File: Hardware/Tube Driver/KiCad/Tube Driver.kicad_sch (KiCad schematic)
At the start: 45 parts, among them J1 I/O, Q1 MMBT3904, Q2 STN2580, Q3 MMBT3904, Q4 MMBT3906, U1 NE555D

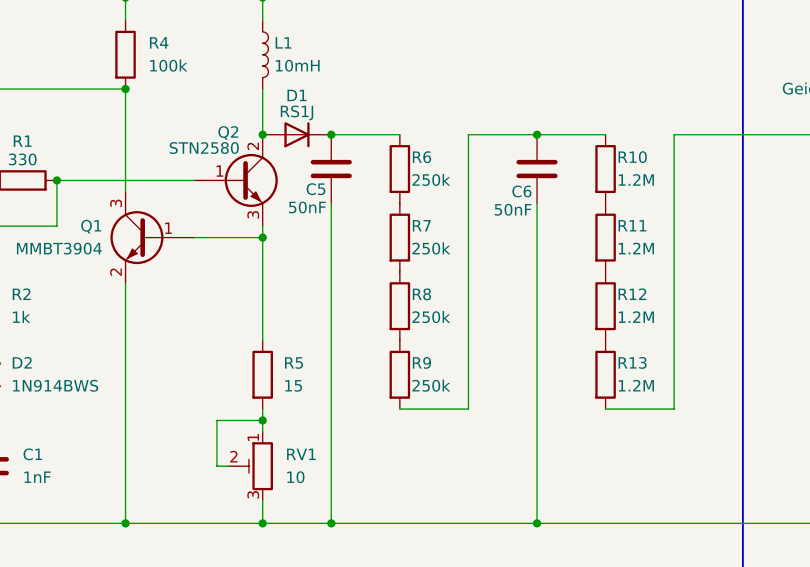
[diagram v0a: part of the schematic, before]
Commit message: Added BoM, updated component values and PCB
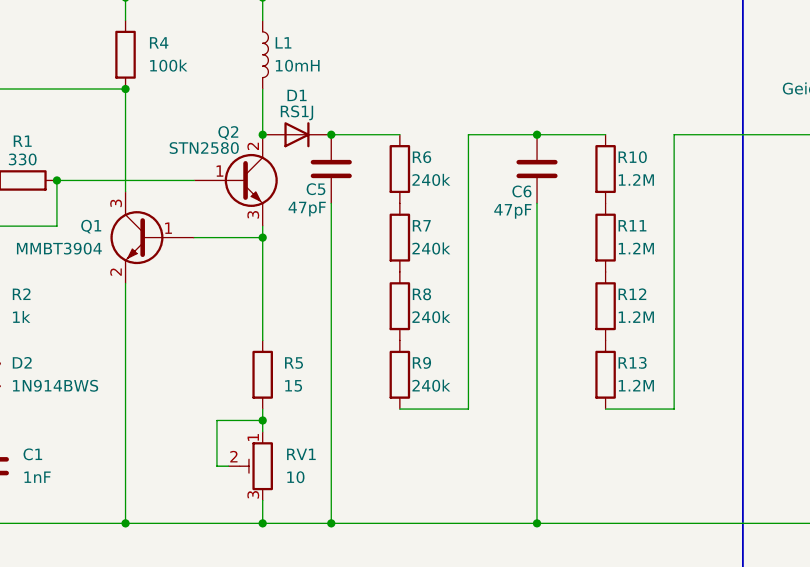
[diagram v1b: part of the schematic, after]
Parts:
- C1: DigiKey (none) -> https://www.digikey.com/en/products/detail/w%C3%BCrth-elekt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; MPN (none) -> 885012208046; Price (EUR) (none) -> 0,09€
- C2, C3: DigiKey (none) -> https://www.digikey.com/en/products/detail/w%C3%BCrth-elekt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; MPN (none) -> 885012208112; Price (EUR) (none) -> 0,1€
- C4: DigiKey (none) -> https://www.digikey.com/en/products/detail/w%C3%BCrth-elekt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; MPN (none) -> 865080243007; Price (EUR) (none) -> 0,25€
- C5, C6: value 50nF -> 47pF; footprint Capacitor_SMD:C_1206_3216Metric_Pad1.33x1.80mm_HandSolder -> Capacitor_SMD:C_1210_3225Metric_Pad1.33x2.70mm_HandSolder; DigiKey (none) -> https://www.digikey.com/en/products/detail/kemet/C1210V473K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; MPN (none) -> C1210V473KDRAC7800; Price (EUR) (none) -> 0,31€
- C7: DigiKey (none) -> https://www.digikey.com/en/products/detail/yageo/CC1206FRNP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; MPN (none) -> CC1206FRNPO9BN821; Price (EUR) (none) -> 0,45€
- D1: DigiKey (none) -> https://www.digikey.com/en/products/detail/diodes-incorpora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; MPN (none) -> RS1J-13-F; Price (EUR) (none) -> 0,4€
- D2: DigiKey (none) -> https://www.digikey.com/en/products/detail/onsemi/1N914BWS/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; MPN (none) -> 1N914BWS; Price (EUR) (none) -> 0,14€
- D3: DigiKey (none) -> https://www.digikey.com/en/products/detail/panjit-internati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; MPN (none) -> RB751V-40_R1_00001; Price (EUR) (none) -> 0,14€
- D4: DigiKey (none) -> https://www.digikey.com/en/products/detail/w%C3%BCrth-elekt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; MPN (none) -> 150120GS75000; Price (EUR) (none) -> 0,2€
- D5: DigiKey (none) -> https://www.digikey.com/en/products/detail/w%C3%BCrth-elekt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; MPN (none) -> 150120RS75000; Price (EUR) (none) -> 0,2€
- GM1: DigiKey (none) -> https://www.digikey.com/en/products/detail/bel-fuse-inc/FC-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; MPN (none) -> FC-102 BRIGHT TIN; Price (EUR) (none) -> 0,1€
- J1: DigiKey (none) -> https://www.digikey.com/en/products/detail/adam-tech/PH2-06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; MPN (none) -> PH2-06-UA; Price (EUR) (none) -> 0,11€
- L1: DigiKey (none) -> https://www.digikey.com/en/products/detail/w%C3%BCrth-elekt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; MPN (none) -> 74404086103; Price (EUR) (none) -> 1,13€
- Q1, Q3: DigiKey (none) -> https://www.digikey.com/en/products/detail/good-ark-semicon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; MPN (none) -> MMBT3904; Price (EUR) (none) -> 0,09€
- Q2: DigiKey (none) -> https://www.digikey.com/en/products/detail/stmicroelectroni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; MPN (none) -> STN2580; Price (EUR) (none) -> 0,48€
- Q4: DigiKey (none) -> https://www.digikey.com/en/products/detail/good-ark-semicon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; MPN (none) -> MMBT3906; Price (EUR) (none) -> 0,09€
- R1: DigiKey (none) -> https://www.digikey.com/en/products/detail/yageo/RC1206FR-0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; MPN (none) -> RC1206FR-07330RL; Price (EUR) (none) -> 0,09€
- R10, R11, R12, R13: DigiKey (none) -> https://www.digikey.com/en/products/detail/yageo/RC1206FR-0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; MPN (none) -> RC1206FR-071M2L; Price (EUR) (none) -> 0,09€
- R14, R15: DigiKey (none) -> https://www.digikey.com/en/products/detail/yageo/RC1206FR-0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; MPN (none) -> RC1206FR-0722KL; Price (EUR) (none) -> 0,09€
- R16, R17, R19: DigiKey (none) -> https://www.digikey.com/en/products/detail/yageo/RC1206FR-1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; MPN (none) -> RC1206FR-1310KL; Price (EUR) (none) -> 0,09€
- R18: DigiKey (none) -> https://www.digikey.com/en/products/detail/yageo/RC1206FR-1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; MPN (none) -> RC1206FR-13150RL; Price (EUR) (none) -> 0,09€
- R2, R20: DigiKey (none) -> https://www.digikey.com/en/products/detail/yageo/RC1206FR-0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; MPN (none) -> RC1206FR-071KL; Price (EUR) (none) -> 0,09€
- R3: DigiKey (none) -> https://www.digikey.com/en/products/detail/yageo/RC1206FR-0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; MPN (none) -> RC1206FR-07220KL; Price (EUR) (none) -> 0,09€
- R4: DigiKey (none) -> https://www.digikey.com/en/products/detail/yageo/AC1206FR-0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; MPN (none) -> AC1206FR-07100KL; Price (EUR) (none) -> 0,09€
- R5: DigiKey (none) -> https://www.digikey.com/en/products/detail/yageo/RC1206FR-0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; MPN (none) -> RC1206FR-0715RL; Price (EUR) (none) -> 0,09€
- R6, R7, R8, R9: value 250k -> 240k; DigiKey (none) -> https://www.digikey.com/en/products/detail/yageo/RC1206FR-0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; MPN (none) -> RC1206FR-07240KL; Price (EUR) (none) -> 0,09€
- RV1: DigiKey (none) -> https://www.digikey.com/en/products/detail/bourns-inc/3361P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; MPN (none) -> 3361P-1-100GLF; Price (EUR) (none) -> 1,14€
- U1: DigiKey (none) -> https://www.digikey.com/en/products/detail/texas-instrument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; MPN (none) -> NE555D; Price (EUR) (none) -> 0,89€

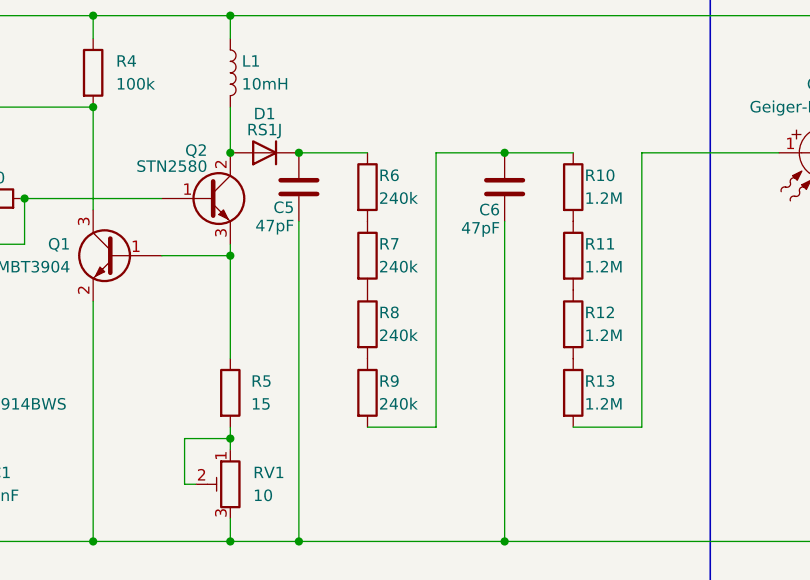
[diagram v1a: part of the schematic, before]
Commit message: Fixed component value typo
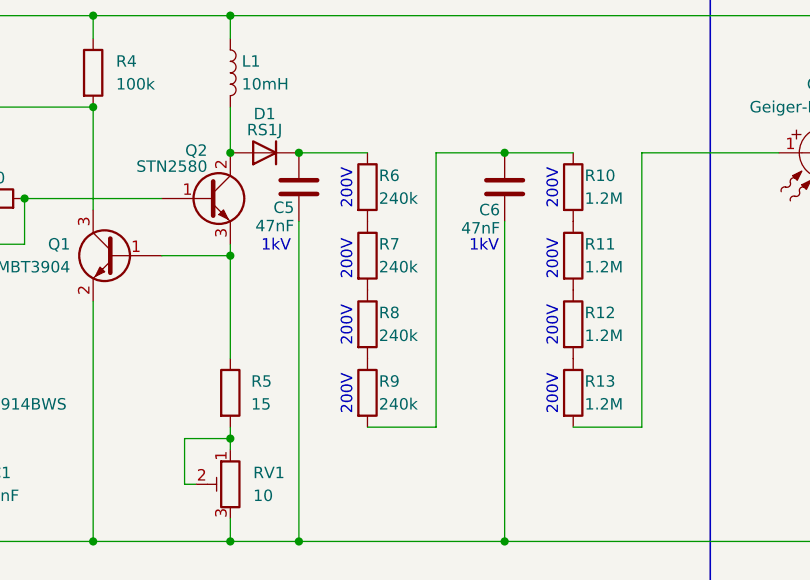
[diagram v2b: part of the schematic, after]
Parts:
- C5, C6: value 47pF -> 47nF
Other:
- note added: "1kV"
- note added: "200V"
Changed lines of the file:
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@@
 	(title_block
 		(title "Tube Driver")
-		(date "2024-09-06")
+		(date "2024-09-10")
 		(rev "1.0")
 		(company "https://github.com/median-dispersion/GMT-Geiger-Counter")
@@
 		)
 	)
+	(text "200V"
+		(exclude_from_sim no)
+		(at 150.114 58.928 90)
+		(effects
+			(font
+				(size 1.27 1.27)
+				(color 0 100 100 1)
+			)
+		)
+	)
+	(text "1kV"
+		(exclude_from_sim no)
+		(at 119.38 57.404 0)
+		(effects
+			(font
+				(size 1.27 1.27)
+				(color 0 100 100 1)
+			)
+		)
+	)
 	(text "GMT"
 		(exclude_from_sim no)
@@
 		)
 	)
+	(text "200V"
+		(exclude_from_sim no)
+		(at 150.114 73.914 90)
+		(effects
+			(font
+				(size 1.27 1.27)
+				(color 0 100 100 1)
+			)
+		)
+	)
+	(text "200V"
+		(exclude_from_sim no)
+		(at 127.254 66.294 90)
+		(effects
+			(font
+				(size 1.27 1.27)
+				(color 0 100 100 1)
+			)
+		)
+	)
+	(text "200V"
+		(exclude_from_sim no)
+		(at 150.114 51.054 90)
+		(effects
+			(font
+				(size 1.27 1.27)
+				(color 0 100 100 1)
+			)
+		)
+	)
 	(text "Pulse Generator & I/O\n"
 		(exclude_from_sim no)
@@
 		)
 	)
+	(text "200V"
+		(exclude_from_sim no)
+		(at 127.254 58.928 90)
+		(effects
+			(font
+				(size 1.27 1.27)
+				(color 0 100 100 1)
+			)
+		)
+	)
+	(text "1kV"
+		(exclude_from_sim no)
+		(at 142.494 57.404 0)
+		(effects
+			(font
+				(size 1.27 1.27)
+				(color 0 100 100 1)
+			)
+		)
+	)
+	(text "200V"
+		(exclude_from_sim no)
+		(at 127.254 51.054 90)
+		(effects
+			(font
+				(size 1.27 1.27)
+				(color 0 100 100 1)
+			)
+		)
+	)
+	(text "200V"
+		(exclude_from_sim no)
+		(at 150.114 66.294 90)
+		(effects
+			(font
+				(size 1.27 1.27)
+				(color 0 100 100 1)
+			)
+		)
+	)
+	(text "200V"
+		(exclude_from_sim no)
+		(at 127.254 73.914 90)
+		(effects
+			(font
+				(size 1.27 1.27)
+				(color 0 100 100 1)
+			)
+		)
+	)
 	(symbol
 		(lib_id "Device:C")
@@
 			)
 		)
-		(property "Value" "47pF"
+		(property "Value" "47nF"
 			(at 144.272 55.372 0)
 			(effects
@@
 			)
 		)
-		(property "Value" "47pF"
+		(property "Value" "47nF"
 			(at 121.412 55.118 0)
 			(effects

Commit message: Updated BoM
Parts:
- R4: DigiKey https://www.digikey.com/en/products/detail/yageo/AC1206FR-0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 -> https://www.digikey.com/en/products/detail/yageo/RC1206FR-0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; MPN AC1206FR-07100KL -> RC1206FR-07100KL
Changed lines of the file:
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@@
 			)
 		)
-		(property "Datasheet" "https://www.yageo.com/upload/media/product/productsearch/datasheet/rchip/PYu-AC_51_RoHS_L_10.pdf"
+		(property "Datasheet" "https://www.yageo.com/upload/media/product/products/datasheet/rchip/PYu-RC_Group_51_RoHS_L_12.pdf"
 			(at 99.06 38.1 0)
 			(effects
@@
 			)
 		)
-		(property "MPN" "AC1206FR-07100KL"
+		(property "MPN" "RC1206FR-07100KL"
 			(at 99.06 38.1 0)
 			(effects
@@
 			)
 		)
-		(property "DigiKey" "https://www.digikey.com/en/products/detail/yageo/AC1206FR-07100KL/2827838"
+		(property "DigiKey" "https://www.digikey.com/en/products/detail/yageo/RC1206FR-07100KL/728492"
 			(at 99.06 38.1 0)
 			(effects

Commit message: Changed component value, fixed typos & fixed small mistakes
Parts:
- C4: DigiKey https://www.digikey.com/en/products/detail/w%C3%BCrth-elekt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 -> https://www.digikey.com/en/products/detail/würth-elektronik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; MPN 865080243007 -> 875105344010; Price (EUR) 0,25€ -> 0,62€
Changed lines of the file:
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@@
 			)
 		)
-		(property "Datasheet" "https://www.we-online.com/components/products/datasheet/865080243007.pdf"
+		(property "Datasheet" "https://www.we-online.com/components/products/datasheet/875105344010.pdf"
 			(at 22.86 38.1 0)
 			(effects
@@
 			)
 		)
-		(property "MPN" "865080243007"
+		(property "MPN" "875105344010"
 			(at 22.86 38.1 0)
 			(effects
@@
 			)
 		)
-		(property "DigiKey" "https://www.digikey.com/en/products/detail/w%C3%BCrth-elektronik/865080243007/5728085"
+		(property "DigiKey" "https://www.digikey.com/en/products/detail/würth-elektronik/875105344010/5147589"
 			(at 22.86 38.1 0)
 			(effects
@@
 			)
 		)
-		(property "Price (EUR)" "0,25€"
+		(property "Price (EUR)" "0,62€"
 			(at 22.86 38.1 0)
 			(effects

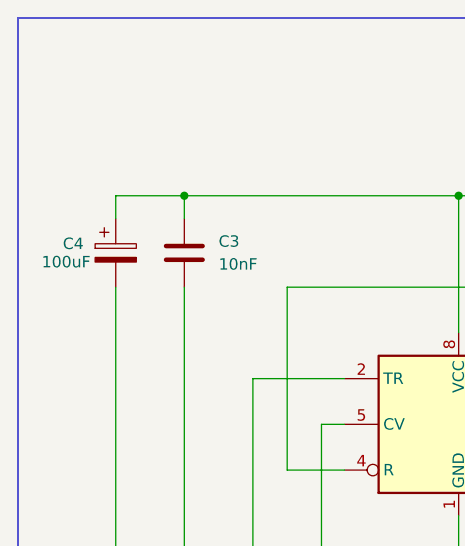
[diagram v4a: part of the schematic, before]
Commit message: Updated the decoupling capacitor to make it more USB 'compliant'
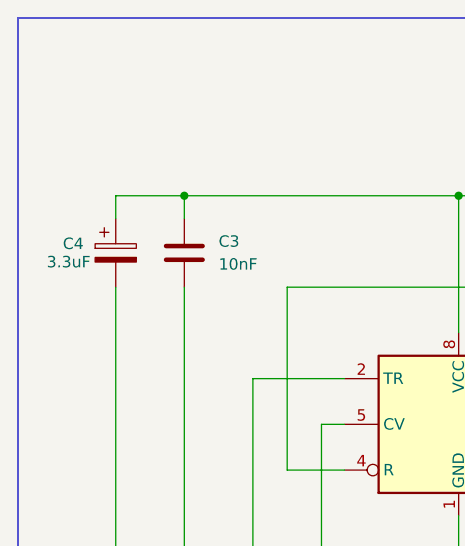
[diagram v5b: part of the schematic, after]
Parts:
- C4: value 100uF -> 3.3uF; DigiKey https://www.digikey.com/en/products/detail/würth-elektronik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 -> https://www.digikey.com/en/products/detail/panasonic-electr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; MPN 875105344010 -> 16SVP3R3M; Price (EUR) 0,62€ -> 0,75€
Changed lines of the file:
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@@
 			)
 		)
-		(property "Value" "100uF"
+		(property "Value" "3.3uF"
 			(at 20.066 39.116 0)
 			(effects
@@
 			)
 		)
-		(property "Datasheet" "https://www.we-online.com/components/products/datasheet/875105344010.pdf"
+		(property "Datasheet" "https://industrial.panasonic.com/ww/products/pt/os-con/models/16SVP3R3M"
 			(at 22.86 38.1 0)
 			(effects
@@
 			)
 		)
-		(property "MPN" "875105344010"
+		(property "MPN" "16SVP3R3M"
 			(at 22.86 38.1 0)
 			(effects
@@
 			)
 		)
-		(property "DigiKey" "https://www.digikey.com/en/products/detail/würth-elektronik/875105344010/5147589"
+		(property "DigiKey" "https://www.digikey.com/en/products/detail/panasonic-electronic-components/16svp3r3m/4204797"
 			(at 22.86 38.1 0)
 			(effects
@@
 			)
 		)
-		(property "Price (EUR)" "0,62€"
+		(property "Price (EUR)" "0,75€"
 			(at 22.86 38.1 0)
 			(effects
